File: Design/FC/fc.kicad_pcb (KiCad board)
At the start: 2 copper layers, 1 part, among them U1 STM32H747BIT6

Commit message: started layout
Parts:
- added BN880_Con1: Conn_01x06, Connector_PinHeader_1.27mm:PinHeader_1x06_P1.27mm_Horizontal, F.Cu at (62.9, 126.9)
- added C1: 100nF, Capacitor_SMD:C_0603_1608Metric_Pad1.08x0.95mm_HandSolder, F.Cu at (256.0, 84.0)
- added C10: 10uF, Capacitor_SMD:C_0603_1608Metric_Pad1.08x0.95mm_HandSolder, F.Cu at (50.4, 84.4)
- added C11: 4.7uF, Capacitor_SMD:C_0603_1608Metric_Pad1.08x0.95mm_HandSolder, F.Cu at (50.4, 86.9)
- added C12: 10uF, Capacitor_SMD:C_0603_1608Metric_Pad1.08x0.95mm_HandSolder, F.Cu at (50.4, 89.4)
- added C13: 1uF, Capacitor_SMD:C_0603_1608Metric_Pad1.08x0.95mm_HandSolder, F.Cu at (50.4, 91.9)
- added C14: 100nF, Capacitor_SMD:C_0603_1608Metric_Pad1.08x0.95mm_HandSolder, F.Cu at (50.0, 94.4)
- added C15: 100nF, Capacitor_SMD:C_0603_1608Metric_Pad1.08x0.95mm_HandSolder, F.Cu at (50.0, 96.9)
- added C16: 100nF, Capacitor_SMD:C_0603_1608Metric_Pad1.08x0.95mm_HandSolder, F.Cu at (50.0, 99.5)
- added C17: 100nF, Capacitor_SMD:C_0603_1608Metric_Pad1.08x0.95mm_HandSolder, F.Cu at (50.0, 102.0)
- added C18: 100nF, Capacitor_SMD:C_0603_1608Metric_Pad1.08x0.95mm_HandSolder, F.Cu at (54.7, 81.9)
- added C19: 100nF, Capacitor_SMD:C_0603_1608Metric_Pad1.08x0.95mm_HandSolder, F.Cu at (54.7, 84.4)
- added C2: 22uF, Lib:CAP_GMK325BJ226MM-T-CAPC3225X280N, F.Cu at (86.5, 97.3)
- added C20: 100nF, Capacitor_SMD:C_0603_1608Metric_Pad1.08x0.95mm_HandSolder, F.Cu at (54.7, 86.9)
- added C21: 100nF, Capacitor_SMD:C_0603_1608Metric_Pad1.08x0.95mm_HandSolder, F.Cu at (54.7, 89.4)
- added C22: 100nF, Capacitor_SMD:C_0603_1608Metric_Pad1.08x0.95mm_HandSolder, F.Cu at (54.7, 91.9)
- added C23: 100nF, Capacitor_SMD:C_0603_1608Metric_Pad1.08x0.95mm_HandSolder, F.Cu at (54.4, 94.4)
- added C24: 100nF, Capacitor_SMD:C_0603_1608Metric_Pad1.08x0.95mm_HandSolder, F.Cu at (54.4, 96.9)
- added C25: 100nF, Capacitor_SMD:C_0603_1608Metric_Pad1.08x0.95mm_HandSolder, F.Cu at (54.4, 99.5)
- added C26: 100nF, Capacitor_SMD:C_0603_1608Metric_Pad1.08x0.95mm_HandSolder, F.Cu at (54.4, 102.0)
- added C27: 100nF, Capacitor_SMD:C_0603_1608Metric_Pad1.08x0.95mm_HandSolder, F.Cu at (59.1, 81.9)
- added C28: 100nF, Capacitor_SMD:C_0603_1608Metric_Pad1.08x0.95mm_HandSolder, F.Cu at (59.1, 84.4)
- added C29: 100nF, Capacitor_SMD:C_0603_1608Metric_Pad1.08x0.95mm_HandSolder, F.Cu at (59.1, 86.9)
- added C3: 22uF, Lib:CAP_GMK325BJ226MM-T-CAPC3225X280N, F.Cu at (86.5, 101.6)
- added C30: 100nF, Capacitor_SMD:C_0603_1608Metric_Pad1.08x0.95mm_HandSolder, F.Cu at (59.1, 89.4)
- added C31: 4.7uF, Capacitor_SMD:C_0603_1608Metric_Pad1.08x0.95mm_HandSolder, F.Cu at (59.1, 91.9)
- added C32: 100nF, Capacitor_SMD:C_0603_1608Metric_Pad1.08x0.95mm_HandSolder, F.Cu at (59.1, 94.4)
- added C34: 2.2uF, Capacitor_SMD:C_0603_1608Metric_Pad1.08x0.95mm_HandSolder, F.Cu at (59.1, 96.9)
- added C35: 2.2uF, Capacitor_SMD:C_0603_1608Metric_Pad1.08x0.95mm_HandSolder, F.Cu at (59.1, 99.5)
- added C36: 100nF, Capacitor_SMD:C_0603_1608Metric_Pad1.08x0.95mm_HandSolder, F.Cu at (59.1, 102.0)
- added C37: 100nF, Capacitor_SMD:C_0603_1608Metric_Pad1.08x0.95mm_HandSolder, F.Cu at (63.4, 81.9)
- added C38: 1uF, Capacitor_SMD:C_0603_1608Metric_Pad1.08x0.95mm_HandSolder, F.Cu at (63.4, 84.4)
- added C39: 100nF, Capacitor_SMD:C_0603_1608Metric_Pad1.08x0.95mm_HandSolder, F.Cu at (63.4, 86.9)
- added C4: 2.2uF, Lib:CAP_C225K4REC7210_0805, F.Cu at (95.0, 88.6)
- added C40: 100nF, Capacitor_SMD:C_0603_1608Metric_Pad1.08x0.95mm_HandSolder, F.Cu at (63.4, 89.4)
- added C41: 2.2uF, Capacitor_SMD:C_0603_1608Metric_Pad1.08x0.95mm_HandSolder, F.Cu at (63.4, 91.9)
- added C42: 100nF, Capacitor_SMD:C_0603_1608Metric_Pad1.08x0.95mm_HandSolder, F.Cu at (50.4, 118.9)
- added C43: 100nF, Capacitor_SMD:C_0603_1608Metric_Pad1.08x0.95mm_HandSolder, F.Cu at (50.4, 121.4)
- added C44: 100nF, Capacitor_SMD:C_0603_1608Metric_Pad1.08x0.95mm_HandSolder, F.Cu at (50.4, 123.9)
- added C45: 1uF, Capacitor_SMD:C_0603_1608Metric_Pad1.08x0.95mm_HandSolder, F.Cu at (50.4, 126.4)
- added C46: 10uF, Capacitor_SMD:C_0603_1608Metric_Pad1.08x0.95mm_HandSolder, F.Cu at (50.4, 128.9)
- added C47: 100nF, Capacitor_SMD:C_0603_1608Metric_Pad1.08x0.95mm_HandSolder, F.Cu at (50.4, 131.4)
- added C48: 100nF, Capacitor_SMD:C_0603_1608Metric_Pad1.08x0.95mm_HandSolder, F.Cu at (50.4, 133.9)
- added C49: 100nF, Capacitor_SMD:C_0603_1608Metric_Pad1.08x0.95mm_HandSolder, F.Cu at (54.7, 118.9)
- added C5: 0.1uF, Lib:CAP_C0805X104K5RAC3316_0805_100nF, F.Cu at (95.0, 82.2)
- added C50: 100uF, Lib:CAP_6.3 X 7.7_PAN, F.Cu at (70.8, 101.7)
- added C51: 2.2uF, Lib:CAP_C225K4REC7210_0805, F.Cu at (95.0, 91.7)
- added C6: 0.1uF, Lib:CAP_C0805X104K5RAC3316_0805_100nF, F.Cu at (95.0, 85.4)
- added C7: 100uF, Lib:CAP_6.3 X 7.7_PAN, F.Cu at (70.8, 84.8)
- added C8: 4.7nF, Capacitor_SMD:C_0805_2012Metric_Pad1.18x1.45mm_HandSolder, F.Cu at (95.8, 101.7)
- added C9: 100uF, Lib:CAP_6.3 X 7.7_PAN, F.Cu at (70.8, 93.3)
- added D1: SD103AW-TP, Lib:SD103AW-TP-SODFL1608X70N, F.Cu at (95.9, 104.3)
- added Debug_Con1: Debug_10_1.27, Connector_PinHeader_1.27mm:PinHeader_2x05_P1.27mm_Vertical, F.Cu at (85.9, 128.5)
- added Debug_UART1: Conn_01x03, Connector_PinHeader_2.54mm:PinHeader_1x03_P2.54mm_Vertical, F.Cu at (50.5, 110.2)
- added FB1: FerriteBead_Small, Lib:MPZ1005S121HT000, F.Cu at (82.8, 77.8)
- added FLASH_1: W25N01GWZEIG, Lib:W25N01GWZEIG, F.Cu at (66.4, 121.4)
- added J1: XT60PW-M, Lib:XT60PW-M, F.Cu at (276.0, 67.0)
- added JL_Servo_2: Conn_01x03, Connector_PinHeader_2.54mm:PinHeader_1x03_P2.54mm_Vertical, F.Cu at (55.1, 110.2)
- added L1: 6.8uH, Lib:IND_SRP1265A-6R8M_BRN, F.Cu at (125.4, 98.5)
- added LED_1: G, LED_SMD:LED_0603_1608Metric, F.Cu at (91.4, 101.5)
- added LED_3: R, LED_SMD:LED_0603_1608Metric, F.Cu at (73.6, 118.9)
- added LED_4: Y, LED_SMD:LED_0603_1608Metric, F.Cu at (73.6, 121.5)
- added LED_5: B, LED_SMD:LED_0603_1608Metric, F.Cu at (73.6, 124.1)
- added LED_6: B, LED_SMD:LED_0603_1608Metric, F.Cu at (73.6, 126.7)
- added LED_7: R, LED_SMD:LED_0603_1608Metric, F.Cu at (73.6, 129.3)
- added LED_8: G, LED_SMD:LED_0603_1608Metric, F.Cu at (91.4, 104.0)
- added L_Motor1: Conn_01x02, Connector_PinHeader_2.54mm:PinHeader_2x01_P2.54mm_Vertical, F.Cu at (77.9, 119.9)
- added L_Servo_1: Conn_01x03, Connector_PinHeader_2.54mm:PinHeader_1x03_P2.54mm_Vertical, F.Cu at (59.7, 110.2)
- added L_Servo_3: Conn_01x03, Connector_PinHeader_2.54mm:PinHeader_1x03_P2.54mm_Vertical, F.Cu at (64.2, 110.2)
- added L_Servo_4: Conn_01x03, Connector_PinHeader_2.54mm:PinHeader_1x03_P2.54mm_Vertical, F.Cu at (68.8, 110.2)
- added R1: 0.01, Lib:RES_PE2512_YAG, F.Cu at (272.5, 89.0)
- added R10: 4.7K, Resistor_SMD:R_0603_1608Metric_Pad0.98x0.95mm_HandSolder, F.Cu at (54.7, 123.9)
- added R11: 4.7K, Resistor_SMD:R_0603_1608Metric_Pad0.98x0.95mm_HandSolder, F.Cu at (54.7, 126.4)
- added R12: 4.7K, Resistor_SMD:R_0603_1608Metric_Pad0.98x0.95mm_HandSolder, F.Cu at (54.7, 128.9)
- added R13: 10K, Resistor_SMD:R_0603_1608Metric_Pad0.98x0.95mm_HandSolder, F.Cu at (54.7, 131.4)
- added R14: 10K, Resistor_SMD:R_0603_1608Metric_Pad0.98x0.95mm_HandSolder, F.Cu at (54.7, 133.9)
- added R15: 330, Resistor_SMD:R_0603_1608Metric_Pad0.98x0.95mm_HandSolder, F.Cu at (59.1, 118.9)
- added R16: 330, Resistor_SMD:R_0603_1608Metric_Pad0.98x0.95mm_HandSolder, F.Cu at (59.1, 121.4)
- added R17: 330, Resistor_SMD:R_0603_1608Metric_Pad0.98x0.95mm_HandSolder, F.Cu at (59.1, 123.9)
- added R18: 330, Resistor_SMD:R_0603_1608Metric_Pad0.98x0.95mm_HandSolder, F.Cu at (59.1, 126.4)
- added R19: 330, Resistor_SMD:R_0603_1608Metric_Pad0.98x0.95mm_HandSolder, F.Cu at (59.1, 128.9)
- added R2: 10k, Lib:RES_ERJ-T06J103V_0805, F.Cu at (93.9, 72.3)
- added R20: 10k, Lib:RES_ERJ-T06J103V_0805, F.Cu at (93.9, 75.3)
- added R3: 240, Resistor_SMD:R_0603_1608Metric_Pad0.98x0.95mm_HandSolder, F.Cu at (63.4, 94.4)
- added R4: 19.6k, Lib:RES_ERJ-PB6B1962V_0805, F.Cu at (94.2, 78.1)
- added R5: 6.8K, Resistor_SMD:R_0805_2012Metric_Pad1.20x1.40mm_HandSolder, F.Cu at (83.5, 72.3)
- added R6: 1.3K, Resistor_SMD:R_0805_2012Metric_Pad1.20x1.40mm_HandSolder, F.Cu at (83.5, 75.3)
- added R7: 560, Resistor_SMD:R_0603_1608Metric_Pad0.98x0.95mm_HandSolder, F.Cu at (63.4, 96.9)
- added R9: 4.7K, Resistor_SMD:R_0603_1608Metric_Pad0.98x0.95mm_HandSolder, F.Cu at (54.7, 121.4)
- added REG_1: MIC26903YJL-TR, Lib:MIC26903YJL-TR-MLF28_5X6_MCH, F.Cu at (297.1, 104.9)
- added REG_2: LD39200PU33R, Lib:LD39200PU33R-SON95P300X300X100-7N, F.Cu at (89.1, 73.2)
- added RF_RECV_CONN1: Conn_01x04, Connector_PinHeader_1.27mm:PinHeader_1x04_P1.27mm_Horizontal, F.Cu at (77.2, 128.5)
- added R_Motor1: Conn_01x02, Connector_PinHeader_2.54mm:PinHeader_2x01_P2.54mm_Vertical, F.Cu at (77.9, 124.5)
- added R_Servo_1: Conn_01x03, Connector_PinHeader_2.54mm:PinHeader_1x03_P2.54mm_Vertical, F.Cu at (73.4, 110.2)
- added R_Servo_2: Conn_01x03, Connector_PinHeader_2.54mm:PinHeader_1x03_P2.54mm_Vertical, F.Cu at (78.0, 110.2)
- added R_Servo_3: Conn_01x03, Connector_PinHeader_2.54mm:PinHeader_1x03_P2.54mm_Vertical, F.Cu at (82.6, 110.2)
- added R_Servo_4: Conn_01x03, Connector_PinHeader_2.54mm:PinHeader_1x03_P2.54mm_Vertical, F.Cu at (87.2, 110.2)
- added U2: INA219AIDCNT, Lib:INA219AIDCNT-SOT65P280X145-8N, F.Cu at (252.2, 86.0)
- added U3: BMI323, Lib:BMI323_BOS, F.Cu at (85.0, 124.5)
- added U4: MMC5983MA, Lib:MMC5983MA_MEM, F.Cu at (85.2, 120.1)
- added U5: BMP390, Lib:BMP390-10LGA_2X2X0p75_BOS, F.Cu at (73.4, 132.5)
- U1: footprint Lib:LQFP-208 -> Lib:STM32H747BIT6-LQFP-208
- moved U1 235.1 mm to (372.8, 174.2)
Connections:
- U1 pad 1: unconnected-(U1B-PE2-Pad1) -> LED_FC_1
- U1 pad 100: unconnected-(U1D-VDD-Pad100) -> +3.3V
- U1 pad 103: unconnected-(U1A-PB14-Pad103) -> USART_1_TX
- U1 pad 104: unconnected-(U1A-PB15-Pad104) -> USART_1_RX
- U1 pad 108: unconnected-(U1D-VDD-Pad108) -> +3.3V
- U1 pad 109: unconnected-(U1D-VSS-Pad109) -> GND
- U1 pad 113: unconnected-(U1D-VSS-Pad113) -> GND
- U1 pad 114: unconnected-(U1D-VDD-Pad114) -> +3.3V
- U1 pad 117: unconnected-(U1D-VDD-Pad117) -> +3.3V
- U1 pad 118: unconnected-(U1D-VSS-Pad118) -> GND
- U1 pad 119: unconnected-(U1D-VCAPDSI-Pad119) -> VDD12DSI
- U1 pad 120: unconnected-(U1D-VDD12DSI-Pad120) -> VDD12DSI
- U1 pad 123: unconnected-(U1D-VSSDSI-Pad123) -> GND
- U1 pad 126: unconnected-(U1D-VDD12DSI-Pad126) -> VDD12DSI
- U1 pad 129: unconnected-(U1D-VSSDSI-Pad129) -> GND
- U1 pad 132: unconnected-(U1D-VSS-Pad132) -> GND
- U1 pad 133: unconnected-(U1D-VDD-Pad133) -> +3.3V
- U1 pad 139: unconnected-(U1D-VSS-Pad139) -> GND
- U1 pad 140: unconnected-(U1D-VDD50USB-Pad140) -> +3.3V
- U1 pad 141: unconnected-(U1D-VDD33USB-Pad141) -> +3.3V
- U1 pad 142: unconnected-(U1A-PC6-Pad142) -> TIM_8_CH_1
- U1 pad 143: unconnected-(U1A-PC7-Pad143) -> TIM_8_CH_2
- U1 pad 144: unconnected-(U1A-PC8-Pad144) -> TIM_8_CH_3
- U1 pad 145: unconnected-(U1A-PC9-Pad145) -> TIM_8_CH_4
- U1 pad 151: unconnected-(U1A-PA13-Pad151) -> DEBUG_SWDIO
- U1 pad 152: unconnected-(U1D-VCAP-Pad152) -> +3.3V
- U1 pad 153: unconnected-(U1D-VSS-Pad153) -> GND
- U1 pad 154: unconnected-(U1D-VDDLDO-Pad154) -> +3.3V
- U1 pad 155: unconnected-(U1D-VDD-Pad155) -> +3.3V
- U1 pad 16: unconnected-(U1D-VSS-Pad16) -> GND
- U1 pad 160: unconnected-(U1D-VSS-Pad160) -> GND
- U1 pad 161: unconnected-(U1D-VDD-Pad161) -> +3.3V
- U1 pad 165: unconnected-(U1A-PA14-Pad165) -> DEBUG_SWCLK
- U1 pad 166: unconnected-(U1A-PA15-Pad166) -> SPI_3_NSS
- U1 pad 167: unconnected-(U1A-PC10-Pad167) -> SPI_3_SCK
- U1 pad 168: unconnected-(U1A-PC11-Pad168) -> SPI_3_MISO
- U1 pad 169: unconnected-(U1A-PC12-Pad169) -> SPI_3_MOSI
- U1 pad 17: unconnected-(U1D-VDD-Pad17) -> +3.3V
- U1 pad 175: unconnected-(U1A-PD5-Pad175) -> USART_2_TX
- U1 pad 176: unconnected-(U1A-PD6-Pad176) -> USART_2_RX
- U1 pad 178: unconnected-(U1D-VSS-Pad178) -> GND
- U1 pad 179: unconnected-(U1D-VDD-Pad179) -> +3.3V
- U1 pad 18: unconnected-(U1D-VSSSMPS-Pad18) -> GND
- U1 pad 186: unconnected-(U1D-VSS-Pad186) -> GND
- U1 pad 187: unconnected-(U1D-VDD-Pad187) -> +3.3V
- U1 pad 189: unconnected-(U1A-PB3-Pad189) -> DEBUG_SWO
- U1 pad 192: unconnected-(U1A-PB6-Pad192) -> I2C_1_SCL
- U1 pad 193: unconnected-(U1A-PB7-Pad193) -> I2C_1_SDA
- U1 pad 194: unconnected-(U1C-BOOT0-Pad194) -> GND
- U1 pad 199: unconnected-(U1D-VCAP-Pad199) -> +3.3V
- U1 pad 2: unconnected-(U1B-PE3-Pad2) -> LED_FC_2
- U1 pad 20: unconnected-(U1D-VDDSMPS-Pad20) -> GND
- U1 pad 200: unconnected-(U1D-VSS-Pad200) -> GND
- U1 pad 202: unconnected-(U1D-VDDLDO-Pad202) -> +3.3V
- U1 pad 205: unconnected-(U1C-PI6-Pad205) -> TIM_8_CH_2
- U1 pad 207: unconnected-(U1D-VSS-Pad207) -> GND
- U1 pad 208: unconnected-(U1D-VDD-Pad208) -> +3.3V
- U1 pad 21: unconnected-(U1D-VFBSDMPS-Pad21) -> GND
- U1 pad 22: unconnected-(U1B-PF0-Pad22) -> I2C_2_SCL
- U1 pad 23: unconnected-(U1B-PF1-Pad23) -> I2C_2_SDA
- U1 pad 25: unconnected-(U1B-PF3-Pad25) -> EXT_3_DEV_INT_BARO
- U1 pad 26: unconnected-(U1B-PF4-Pad26) -> SPI_5_NSS_BARO
- U1 pad 28: unconnected-(U1D-VSS-Pad28) -> GND
- U1 pad 29: unconnected-(U1D-VDD-Pad29) -> +3.3V
- U1 pad 3: unconnected-(U1B-PE4-Pad3) -> LED_FC_3
- U1 pad 30: unconnected-(U1B-PF6-Pad30) -> EXT_6_DEV_INT_MAG
- U1 pad 31: unconnected-(U1B-PF7-Pad31) -> SPI_5_SCK
- U1 pad 32: unconnected-(U1B-PF8-Pad32) -> SPI_5_MISO
- U1 pad 33: unconnected-(U1B-PF9-Pad33) -> SPI_5_MOSI
- U1 pad 34: unconnected-(U1B-PF10-Pad34) -> SPI_5_NSS_MAG
- U1 pad 37: unconnected-(U1C-NRST-Pad37) -> NRST
- U1 pad 4: unconnected-(U1B-PE5-Pad4) -> LED_FC_4
- U1 pad 42: unconnected-(U1D-VSSA-Pad42) -> GND
- U1 pad 43: unconnected-(U1D-VREF+-Pad43) -> VDDA_MCU
- U1 pad 44: unconnected-(U1D-VDDA-Pad44) -> VDDA_MCU
- U1 pad 45: unconnected-(U1A-PA0-Pad45) -> TIM_5_CH_1
- U1 pad 46: unconnected-(U1A-PA1-Pad46) -> TIM_5_CH_2
- U1 pad 47: unconnected-(U1A-PA2-Pad47) -> TIM_5_CH_3
- U1 pad 49: unconnected-(U1D-VDD-Pad49) -> +3.3V
- U1 pad 5: unconnected-(U1B-PE6-Pad5) -> LED_FC_5
- U1 pad 50: unconnected-(U1D-VSS-Pad50) -> GND
- U1 pad 54: unconnected-(U1A-PA3-Pad54) -> TIM_5_CH_4
- U1 pad 55: unconnected-(U1D-VSS-Pad55) -> GND
- U1 pad 56: unconnected-(U1D-VDD-Pad56) -> +3.3V
- U1 pad 58: unconnected-(U1A-PA5-Pad58) -> SPI_1_SCK
- U1 pad 59: unconnected-(U1A-PA6-Pad59) -> SPI_1_MISO
- U1 pad 6: unconnected-(U1D-VSS-Pad6) -> GND
- U1 pad 60: unconnected-(U1A-PA7-Pad60) -> SPI_1_MOSI
- U1 pad 61: unconnected-(U1A-PC4-Pad61) -> SPI_1_NSS_IMU
- U1 pad 62: unconnected-(U1A-PC5-Pad62) -> EXT_5_DEV_IMU
- U1 pad 7: unconnected-(U1D-VDD-Pad7) -> +3.3V
- U1 pad 73: unconnected-(U1D-VSS-Pad73) -> GND
- U1 pad 74: unconnected-(U1D-VDD-Pad74) -> +3.3V
- U1 pad 79: unconnected-(U1D-VSS-Pad79) -> GND
- U1 pad 8: unconnected-(U1D-VBAT-Pad8) -> +3.3V
- U1 pad 80: unconnected-(U1D-VDD-Pad80) -> +3.3V
- U1 pad 87: unconnected-(U1A-PB10-Pad87) -> USART_3_TX
- U1 pad 88: unconnected-(U1A-PB11-Pad88) -> USART_3_RX
- U1 pad 89: unconnected-(U1D-VCAP-Pad89) -> +3.3V
- U1 pad 90: unconnected-(U1D-VSS-Pad90) -> GND
- U1 pad 91: unconnected-(U1D-VDDLDO-Pad91) -> +3.3V
- U1 pad 92: unconnected-(U1B-PH6-Pad92) -> TIM_12_CH_1
- U1 pad 98: unconnected-(U1B-PH12-Pad98) -> TIM_12_CH_2
- U1 pad 99: unconnected-(U1D-VSS-Pad99) -> GND
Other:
- copper layers 2 -> 4

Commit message: started laying out voltage regulator
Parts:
- C4, C5, C51, C6, D1, R20, R4, R5, R6: moved to B.Cu
- moved R_Servo_1 236.0 mm to (305.5, 153.0), turned to -90 degrees
- moved R_Servo_2 232.4 mm to (305.5, 158.0), turned to -90 degrees
- moved R_Motor1 230.3 mm to (303.0, 173.0), turned to 180 degrees
- moved R_Servo_3 229.0 mm to (305.5, 163.0), turned to -90 degrees
- moved Debug_UART1 226.3 mm to (260.5, 194.5), turned to 90 degrees
- moved R_Servo_4 225.8 mm to (305.5, 168.0), turned to -90 degrees
- moved C13 192.8 mm to (224.6, 174.5)
- moved BN880_Con1 190.8 mm to (242.2, 192.0), turned to -90 degrees
- moved C20 190.1 mm to (229.3, 162.0), turned to 180 degrees
- moved C18 189.4 mm to (229.1, 155.8), turned to 180 degrees
- moved C19 189.1 mm to (229.1, 157.5), turned to 180 degrees
- moved C32 188.0 mm to (229.1, 174.5)
- moved C44 186.8 mm to (223.1, 195.0)
- moved C43 186.6 mm to (223.1, 192.0)
- moved C42 186.0 mm to (229.3, 169.5), turned to 180 degrees
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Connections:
- net Net-(D1-A) renamed /Power/REG_1_VDD
- net Net-(REG_1-PVDD) renamed /Power/REG_1_PVDD
- C2 pad 1: +BATT -> REG_1_VIN
- C3 pad 1: +BATT -> REG_1_VIN
- C42 pad 1: +3.3V -> NRST
- C50 pad 1: +BATT -> REG_1_VIN
- C6 pad 2: REG_1_SW -> REG_1_CS
- Debug_Con1 pad 1: Net-(Debug_Con1-Pin_1) -> +3.3V
- Debug_Con1 pad 10: Net-(Debug_Con1-Pin_10) -> NRST
- R1 pad 2: VIN- -> REG_1_VIN
- R10 pad 2: I2C_1_SCL -> CURRENT_SENSE_SCL
- R11 pad 2: I2C_2_SCL -> GPS_SCL
- R12 pad 2: I2C_2_SDA -> GPS_SDA
- R2 pad 1: +BATT -> REG_1_VIN
- R9 pad 2: I2C_1_SDA -> CURRENT_SENSE_SDA
- REG_1 pad 10: REG_1_SW -> REG_1_CS
- REG_1 pad 11: REG_1_SW -> REG_1_CS
- REG_1 pad 12: REG_1_SW -> REG_1_CS
- REG_1 pad 4: REG_1_SW -> REG_1_CS
- REG_1 pad 9: REG_1_SW -> REG_1_CS
- U1 pad 103: USART_1_TX -> DEBUG_TX
- U1 pad 104: USART_1_RX -> DEBUG_RX
- U1 pad 142: TIM_8_CH_1 -> R_SERVO_1_SIGNAL
- U1 pad 143: TIM_8_CH_2 -> R_SERVO_2_SIGNAL
- U1 pad 144: TIM_8_CH_3 -> R_SERVO_3_SIGNAL
- U1 pad 145: TIM_8_CH_4 -> R_SERVO_4_SIGNAL
- U1 pad 166: SPI_3_NSS -> FLASH_1_NSS
- U1 pad 167: SPI_3_SCK -> FLASH_1_SCK
- U1 pad 168: SPI_3_MISO -> FLASH_1_MISO
- U1 pad 169: SPI_3_MOSI -> FLASH_1_MOSI
- U1 pad 175: USART_2_TX -> RF_RECV_TX
- U1 pad 176: USART_2_RX -> RF_RECV_RX
- U1 pad 192: I2C_1_SCL -> CURRENT_SENSE_SCL
- U1 pad 193: I2C_1_SDA -> CURRENT_SENSE_SDA
- U1 pad 205: TIM_8_CH_2 -> R_SERVO_2_SIGNAL
- U1 pad 22: I2C_2_SCL -> GPS_SCL
- U1 pad 23: I2C_2_SDA -> GPS_SDA
- U1 pad 25: EXT_3_DEV_INT_BARO -> BARO_SPI_NSS
- U1 pad 26: SPI_5_NSS_BARO -> BARO_INT_1
- U1 pad 31: SPI_5_SCK -> BARO_SPI_SCK
- U1 pad 32: SPI_5_MISO -> BARO_SPI_MISO
- U1 pad 33: SPI_5_MOSI -> BARO_SPI_MOSI
- U1 pad 34: SPI_5_NSS_MAG -> MAG_SPI_NSS
- U1 pad 45: TIM_5_CH_1 -> L_SERVO_1_SIGNAL
- U1 pad 46: TIM_5_CH_2 -> L_SERVO_2_SIGNAL
- U1 pad 47: TIM_5_CH_3 -> L_SERVO_3_SIGNAL
- U1 pad 54: TIM_5_CH_4 -> L_SERVO_4_SIGNAL
- U1 pad 58: SPI_1_SCK -> IMU_SPI_SCK
- U1 pad 59: SPI_1_MISO -> IMU_SPI_MISO
- U1 pad 60: SPI_1_MOSI -> IMU_SPI_MOSI
- U1 pad 61: SPI_1_NSS_IMU -> IMU_SPI_NSS
- U1 pad 87: USART_3_TX -> GPS_TX
- U1 pad 88: USART_3_RX -> GPS_RX
- U1 pad 92: TIM_12_CH_1 -> L_MOTOR_1_SIGNAL
- U1 pad 98: TIM_12_CH_2 -> R_MOTOR_1_SIGNAL
- U2 pad 2: VIN- -> REG_1_VIN
- U3 pad 4: IMU_INT_1 -> EXT_5_DEV_IMU
- U4 pad 1: MAG_SPI_SCK -> BARO_SPI_SCK
- U4 pad 15: MAG_INT_1 -> EXT_6_DEV_INT_MAG
- U4 pad 16: MAG_SPI_MOSI -> BARO_SPI_MOSI
- U4 pad 5: MAG_SPI_MISO -> BARO_SPI_MISO
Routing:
- net REG_1_VIN: track 0.00 -> 37.2 mm, vias 0 -> 1
- net GND: track 0.00 -> 15.0 mm
- net REG_1_EN: track 0.00 -> 3.98 mm, vias 0 -> 1
- net REG_1_FB: track 0.00 -> 0.20 mm, vias 0 -> 1
- net REG_1_PG: vias 0 -> 1
- net REG_1_CS: vias 0 -> 2
- net REG_1_BST: vias 0 -> 1
- net /Power/REG_1_VDD: vias 0 -> 1
- net /Power/REG_1_PVDD: vias 0 -> 1
- net +5V: vias 0 -> 1
- added copper zone on F.Cu, net GND
- added copper zone on F.Cu, net REG_1_CS
- added copper zone on F.Cu, net REG_1_VIN
- added copper zone on F.Cu, net VIN+

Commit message: before shrinking pcb
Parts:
- added H1: MountingHole, MountingHole:MountingHole_3.2mm_M3_Pad_Via, F.Cu at (139.0, 57.0)
- added H2: MountingHole_Pad, MountingHole:MountingHole_3.2mm_M3_Pad_Via, F.Cu at (139.0, 144.1)
- added H3: MountingHole, MountingHole:MountingHole_3.2mm_M3_Pad_Via, F.Cu at (227.0, 144.1)
- added H4: MountingHole_Pad, MountingHole:MountingHole_3.2mm_M3_Pad_Via, F.Cu at (227.0, 57.0)
- added NT1: NT, Lib:NetTie-2_SMD_Track0.35mm, F.Cu at (202.6, 123.8)
- added NT2: NT, Lib:NetTie-2_SMD_Track0.35mm, F.Cu at (203.6, 126.6)
- added NT3: NT, Lib:NetTie-2_SMD_Track0.35mm, F.Cu at (213.9, 108.1)
- added NT4: NT, Lib:NetTie-2_SMD_Track0.35mm, F.Cu at (213.8, 101.2)
- added NT5: NT, Lib:NetTie-2_SMD_Track0.35mm, F.Cu at (178.9, 114.7)
- added NT6: NT, Lib:NetTie-2_SMD_Track0.35mm, F.Cu at (179.2, 98.2)
- added NT7: NT, Lib:NetTie-2_SMD_Track0.35mm, F.Cu at (175.2, 110.0)
- added NT8: NT, Lib:NetTie-2_SMD_Track0.35mm, F.Cu at (190.6, 90.0)
- C8: moved to B.Cu
- moved C45 106.2 mm to (163.5, 103.4), turned to 90 degrees
- moved RF_RECV_CONN1 103.8 mm to (187.9, 55.8)
- moved C46 103.3 mm to (166.0, 102.6), turned to 180 degrees
- moved U4 99.5 mm to (166.2, 105.5), turned to 90 degrees
- moved R_Servo_4 93.6 mm to (231.1, 111.2)
- moved R_Servo_3 88.0 mm to (231.1, 116.0)
- moved C36 87.4 mm to (178.4, 97.7), turned to 180 degrees
- moved U5 86.9 mm to (165.7, 112.4), turned to 180 degrees
- moved R_Motor1 86.9 mm to (228.5, 128.4)
- moved C17 86.3 mm to (194.4, 88.3), turned to 90 degrees
- moved C48 83.6 mm to (165.4, 114.8), turned to 180 degrees
- moved R_Servo_2 83.3 mm to (231.2, 120.4)
- moved C47 82.5 mm to (168.8, 113.8)
- moved C32 81.6 mm to (174.0, 114.3), turned to 180 degrees
- moved C11 81.1 mm to (181.9, 89.5), turned to 90 degrees
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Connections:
- C31 pad 1: +3.3V -> /Power/VDD_LDO
- C34 pad 1: +3.3V -> /Power/VCAP
- C35 pad 1: +3.3V -> /Power/VCAP
- C36 pad 1: +3.3V -> /Power/VBAT
- C37 pad 1: VDDA_MCU -> /Power/VREF+
- C38 pad 1: VDDA_MCU -> /Power/VREF+
- C39 pad 1: +3.3V -> /Power/VDDUSB
- C40 pad 1: +3.3V -> /Power/VDDUSB
- C41 pad 1: VDD12DSI -> /Power/VCAPDSI
- REG_1 pad 30: REG_1_CS -> (no net)
- REG_1 pad 31: REG_1_VIN -> (no net)
- REG_1 pad 32: GND -> (no net)
- U1 pad 119: VDD12DSI -> /Power/VCAPDSI
- U1 pad 140: +3.3V -> /Power/VDDUSB
- U1 pad 141: +3.3V -> /Power/VDDUSB
- U1 pad 152: +3.3V -> /Power/VCAP
- U1 pad 154: +3.3V -> /Power/VDD_LDO
- U1 pad 194: GND -> /Flight Controller/BOOT0
- U1 pad 199: +3.3V -> /Power/VCAP
- U1 pad 202: +3.3V -> /Power/VDD_LDO
- U1 pad 205: R_SERVO_2_SIGNAL -> unconnected-(U1C-PI6-Pad205)
- U1 pad 25: BARO_SPI_NSS -> EXT_3_DEV_INT
- U1 pad 26: BARO_INT_1 -> MAG_SPI_NSS
- U1 pad 30: EXT_6_DEV_INT_MAG -> BARO_SPI_NSS
- U1 pad 34: MAG_SPI_NSS -> BARO_INT_1
- U1 pad 43: VDDA_MCU -> /Power/VREF+
- U1 pad 8: +3.3V -> /Power/VBAT
- U1 pad 89: +3.3V -> /Power/VCAP
- U1 pad 91: +3.3V -> /Power/VDD_LDO
- U4 pad 15: EXT_6_DEV_INT_MAG -> EXT_3_DEV_INT
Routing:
- net +5V: track 0.00 -> 85.8 mm, vias 1 -> 27
- net /Power/VCAP: track 0.00 -> 75.6 mm, vias 0 -> 4
- net +3.3V: track 0.00 -> 74.4 mm, vias 0 -> 26
- net NRST: track 0.00 -> 65.3 mm, vias 0 -> 2
- net /Power/VDD_LDO: track 0.00 -> 54.9 mm
- net GND: track 15.0 -> 66.1 mm, vias 0 -> 26
- net RF_RECV_TX: track 0.00 -> 41.0 mm, vias 0 -> 2
- net DEBUG_SWO: track 0.00 -> 40.4 mm, vias 0 -> 2
- net RF_RECV_RX: track 0.00 -> 40.0 mm, vias 0 -> 2
- net DEBUG_SWCLK: track 0.00 -> 27.2 mm
- net REG_1_CS: track 0.00 -> 27.0 mm
- net BARO_SPI_NSS: track 0.00 -> 25.3 mm, vias 0 -> 2
- net BARO_INT_1: track 0.00 -> 24.9 mm, vias 0 -> 2
- net EXT_3_DEV_INT: track 0.00 -> 22.8 mm, vias 0 -> 2
- net BARO_SPI_MISO: track 0.00 -> 22.7 mm, vias 0 -> 2
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- added copper zone on In2.Cu, net +5V
- added copper zone on B.Cu, net GND
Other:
- board outline added: 100 x 100 mm

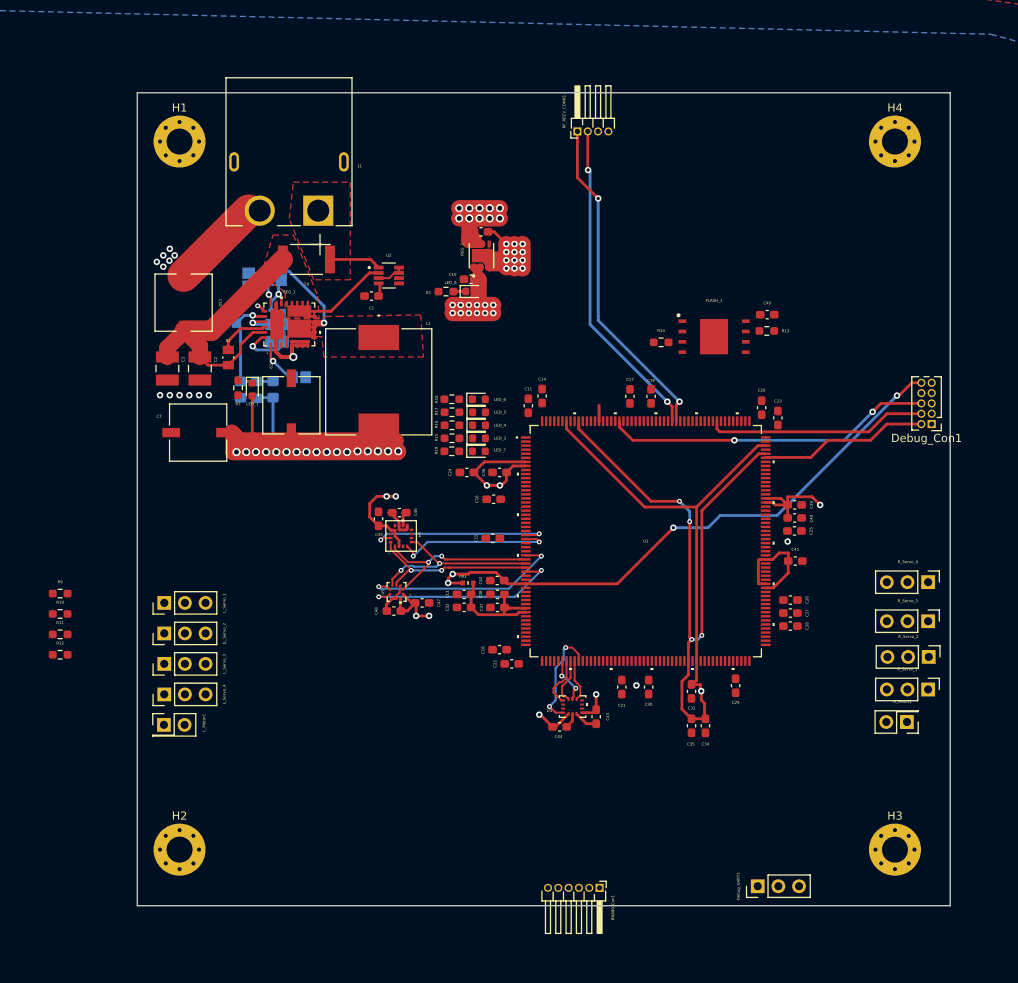
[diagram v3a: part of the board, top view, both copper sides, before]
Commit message: finished pcb layout and started on bom
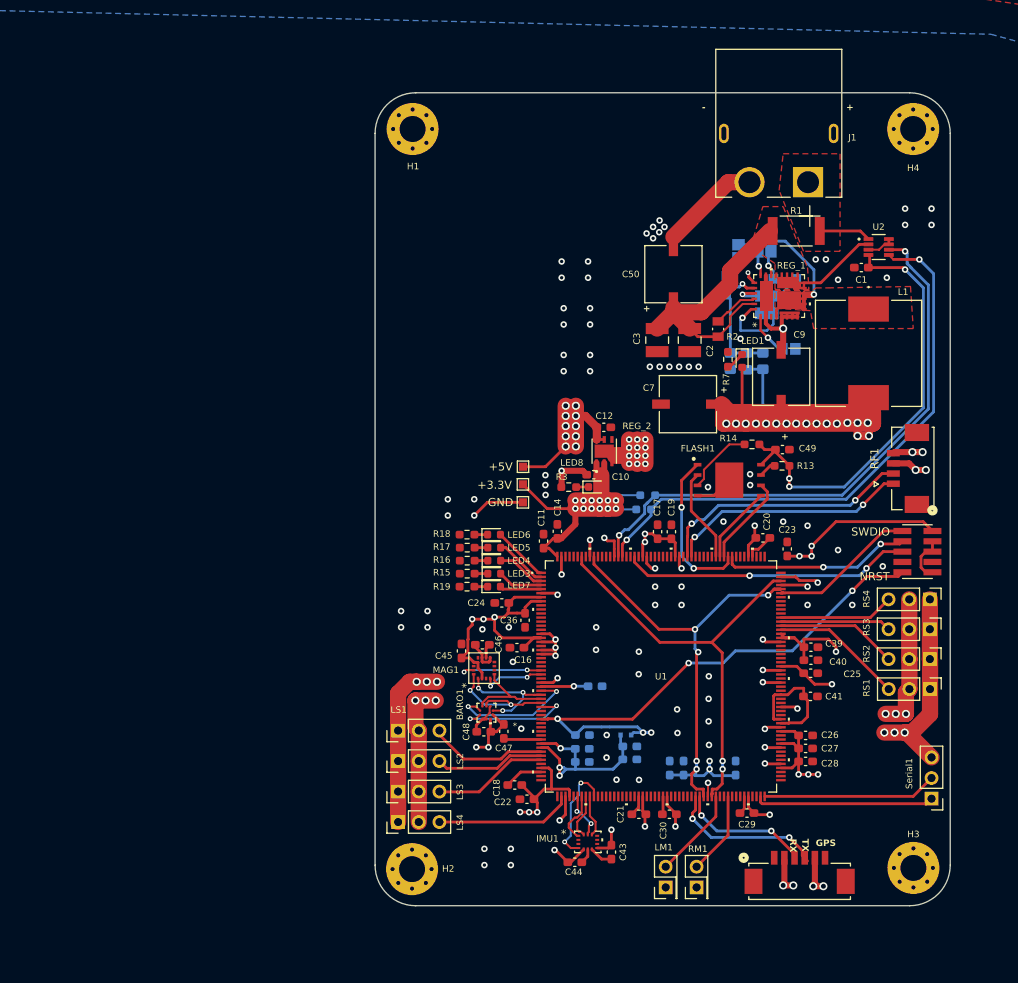
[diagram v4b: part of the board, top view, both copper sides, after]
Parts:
- removed R11, R12: 4.7K, Resistor_SMD:R_0603_1608Metric_Pad0.98x0.95mm_HandSolder
- added +3.3V: TestPoint_Pad_1.0x1.0mm, TestPoint:TestPoint_Pad_1.0x1.0mm, F.Cu at (181.2, 99.2)
- added +5V: TestPoint_Pad_1.0x1.0mm, TestPoint:TestPoint_Pad_1.0x1.0mm, F.Cu at (181.2, 97.0)
- added GND: TestPoint_Pad_1.0x1.0mm, TestPoint:TestPoint_Pad_1.0x1.0mm, F.Cu at (181.2, 101.4)
- C13, C15, C31, C32, C34, C35, C37, C38, C42, FB1, NT1, NT2, NT5, NT7, R10, R9: moved to B.Cu
- D1: footprint Lib:SD103AW-TP-SODFL1608X70N -> Diode_SMD:Nexperia_CFP3_SOD-123W
- FLASH1: renamed from FLASH_1; value W25N01GWZEIG -> SON127P800X600X80-9N-D
- GPS1: renamed from BN880_Con1; footprint Connector_PinHeader_1.27mm:PinHeader_1x06_P1.27mm_Horizontal -> Molex:CONN_532610001-SD_06Pin_1.25mm
- J1: value XT60PW-M -> AMASS_XT60PW-M
- REG_2: footprint Lib:LD39200PU33R-SON95P300X300X100-7N -> Regulators:SON95P300X300X100-7N
- RF1: renamed from RF_RECV_CONN1; footprint Connector_PinHeader_1.27mm:PinHeader_1x04_P1.27mm_Horizontal -> Molex:CONN_532610471_SMD_4Pin_1.25mm
- SWD1: renamed from Debug_Con1; footprint Connector_PinHeader_1.27mm:PinHeader_2x05_P1.27mm_Vertical -> Connectors:CONN_GRPB052VWQS-RC_OddEven_2x5Pins_1.27mm
- moved R9 73.3 mm to (196.6, 100.5)
- moved R10 72.9 mm to (196.1, 102.2)
- moved LM1 64.9 mm to (198.8, 148.7), turned to 90 degrees
- moved D1 62.6 mm to (213.5, 73.9)
- moved C1 60.4 mm to (222.9, 72.5)
- moved C2 60.4 mm to (201.8, 81.4)
- moved C3 60.4 mm to (197.8, 81.4)
- moved C4 60.4 mm to (213.9, 82.5)
- moved C5 60.4 mm to (207.8, 70.5)
- moved C50 60.4 mm to (199.8, 73.3)
- moved C51 60.4 mm to (211.2, 78.1)
- moved C6 60.4 mm to (210.9, 70.5)
- moved C7 60.4 mm to (201.5, 89.3)
- moved C8 60.4 mm to (208.8, 84.0)
- moved C9 60.4 mm to (213.0, 85.9)
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- renumbered U5 to BARO1, U3 to IMU1, LED_1 to LED1, LED_3 to LED3, LED_4 to LED4, LED_5 to LED5, LED_6 to LED6, LED_7 to LED7, LED_8 to LED8, L_Motor1 to LM1, L_Servo_1 to LS1, JL_Servo_2 to LS2, L_Servo_3 to LS3, L_Servo_4 to LS4, U4 to MAG1, R_Motor1 to RM1, R_Servo_1 to RS1, R_Servo_2 to RS2, R_Servo_3 to RS3, R_Servo_4 to RS4, Debug_UART1 to Serial1
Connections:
- GPS1 pad 1: GPS_SDA -> unconnected-(GPS1-Pin_1-Pad1)
- GPS1 pad 6: GPS_SCL -> unconnected-(GPS1-Pin_6-Pad6)
- U1 pad 22: GPS_SCL -> unconnected-(U1B-PF0-Pad22)
- U1 pad 23: GPS_SDA -> unconnected-(U1B-PF1-Pad23)
- U1 pad 95: unconnected-(U1B-PH9-Pad95) -> R_MOTOR_1_SIGNAL
- U1 pad 98: R_MOTOR_1_SIGNAL -> unconnected-(U1B-PH12-Pad98)
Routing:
- net +3.3V: track 74.4 -> 256.5 mm, vias 26 -> 45
- net GND: track 66.1 -> 207.9 mm, vias 26 -> 125
- net CURRENT_SENSE_SCL: track 0.00 -> 70.4 mm, vias 0 -> 2
- net CURRENT_SENSE_SDA: track 0.00 -> 70.1 mm, vias 0 -> 2
- net +5V: track 85.8 -> 139.3 mm, vias 27 -> 37
- net DEBUG_TX: track 0.00 -> 22.1 mm
- net DEBUG_RX: track 0.00 -> 21.5 mm
- net GPS_TX: track 0.00 -> 19.8 mm, vias 0 -> 2
- net FLASH_1_NSS: track 0.00 -> 19.5 mm, vias 0 -> 2
- net /Power/VCAP: track 75.6 -> 56.6 mm, vias 4 -> 5
- net L_SERVO_4_SIGNAL: track 0.00 -> 16.9 mm
- net GPS_RX: track 0.00 -> 16.3 mm, vias 0 -> 2
- net R_SERVO_1_SIGNAL: track 0.00 -> 16.3 mm
- net R_SERVO_2_SIGNAL: track 0.00 -> 14.9 mm
- net L_SERVO_1_SIGNAL: track 0.00 -> 14.6 mm
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- added copper zone on In2.Cu, net +3.3V
- added copper zone on In1.Cu, net GND
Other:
- board size 100 x 100 mm -> 70.8 x 100 mm
- board text added: "+"
- board text added: "-"
- board text added: "GND +5V PWM"
- board text added: "GND PWM"
- board text added: "GPS"
- board text added: "NRST"
- board text added: "PWM +5V GND"
- board text added: "RX"
- board text added: "SWDIO"
- board text added: "TX"
- board text added: "TX RX GND"
